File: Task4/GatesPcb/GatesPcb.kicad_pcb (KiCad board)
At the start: 2 copper layers, 73.4 x 42.7 mm, 56 parts, among them J1 Photodiode1_(+), J10 sw2, J11 sw1_PWR, J12 sw1, J13 rst_btn_gnd, J14 OTA_(+), J15 OTA_(-), J16 Laser_Mode_(-), J17 Laser_Mode_(+), J18 Btn_Mode_(-), J19 Btn_Mode_(+), J2 Photodiode1_(-), J20 Speaker_Mode_(-), J21 Speaker_Mode_(+), J22 sw2_PWR, J23 on_off_ldo, J24 rst_btn_en, J25 usr_btn_sig, J26 usr_btn_vdd, J27 Audio_P, J28 Audio_N, J3 Photodiode2_(-), J4 Photodiode2_(+), J5 on_off_bat, J6 Photodiode1Indicator_(+), J7 Photodiode1Indicator_(-), J8 Photodiode2Indicator_(+), J9 Photodiode2Indicator_(-), U1 ESP32-S2-SOLO, U2 LM317_SOT-223, U3 UART, U4 MAX98357A, U5 BOOT

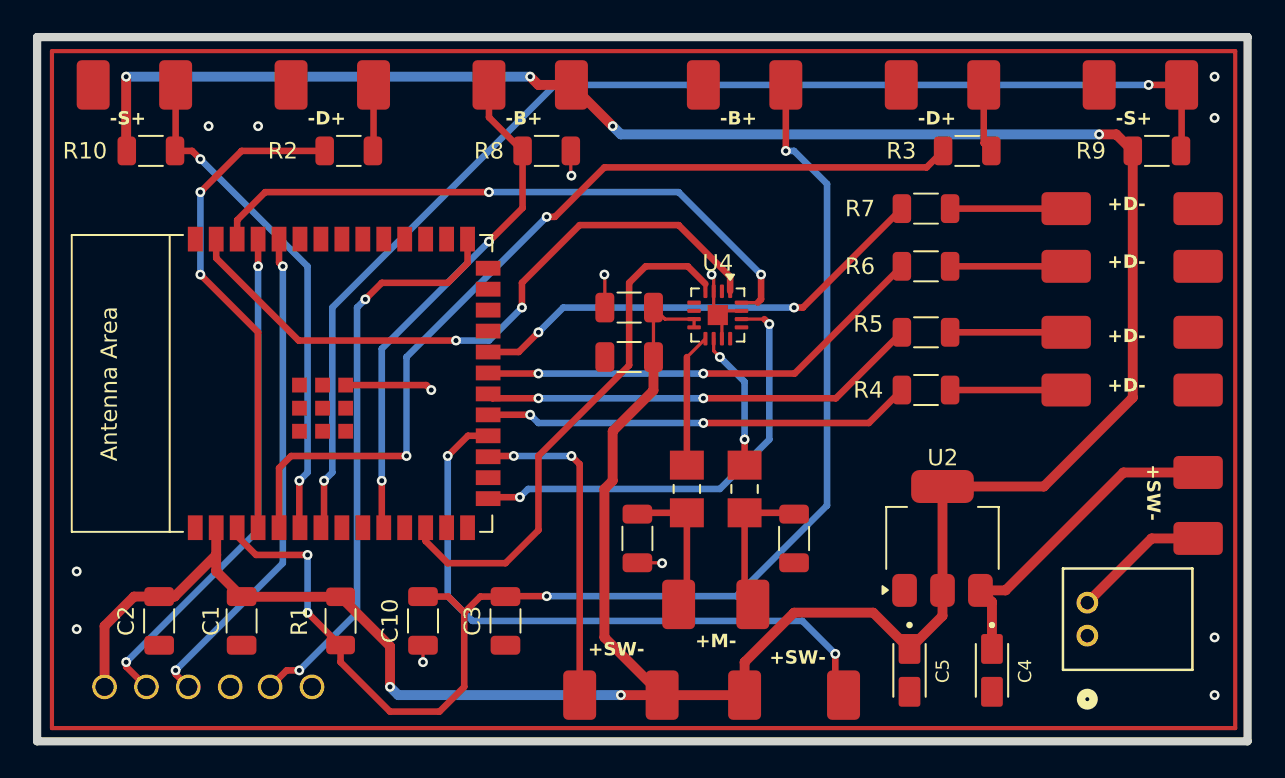
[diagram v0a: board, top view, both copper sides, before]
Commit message: pcb routing correction
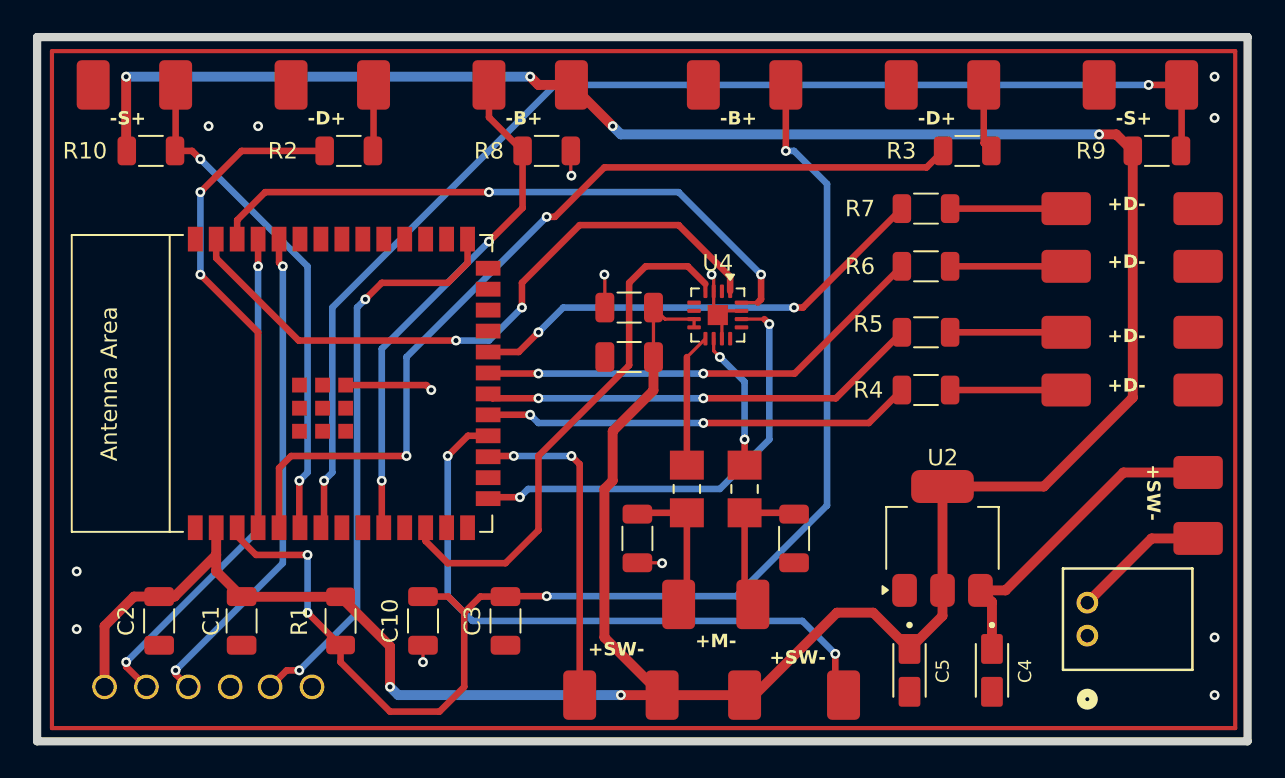
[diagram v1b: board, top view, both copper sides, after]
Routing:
- net VDD: track 201.9 -> 200.7 mm
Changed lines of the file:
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@@
-	)
-	(segment
-		(start 131.5 105)
-		(end 128.5 108)
-		(width 0.6)
-		(layer "F.Cu")
-		(net 1)
 	)
 	(segment
@@
 	)
 	(segment
+		(start 136.3 105)
+		(end 134.1 105)
+		(width 0.6)
+		(layer "F.Cu")
+		(net 1)
+	)
+	(segment
 		(start 140.5 97.35)
 		(end 140.5 103.65)
@@
 	)
 	(segment
+		(start 134.1 105)
+		(end 129.1 110)
+		(width 0.6)
+		(layer "F.Cu")
+		(net 1)
+	)
+	(segment
 		(start 125.4375 87.2)
 		(end 125.4375 87.7)
@@
 	)
 	(segment
+		(start 129.1 110)
+		(end 128.5 110)
+		(width 0.6)
+		(layer "F.Cu")
+		(net 1)
+	)
+	(segment
 		(start 123.5 110)
 		(end 121 110)
@@
 	)
 	(segment
-		(start 128.5 108)
-		(end 128.5 110)
-		(width 0.6)
-		(layer "F.Cu")
-		(net 1)
-	)
-	(segment
 		(start 152.0375 91.9625)
 		(end 152.0375 77)
@@
 	)
 	(segment
+		(start 96.46 102.485)
+		(end 96.46 101.5)
+		(width 0.6)
+		(layer "F.Cu")
+		(net 1)
+	)
+	(segment
 		(start 138.5 107.2)
 		(end 136.3 105)
-		(width 0.6)
-		(layer "F.Cu")
-		(net 1)
-	)
-	(segment
-		(start 96.46 102.485)
-		(end 96.46 101.5)
-		(width 0.6)
-		(layer "F.Cu")
-		(net 1)
-	)
-	(segment
-		(start 136.3 105)
-		(end 131.5 105)
 		(width 0.6)
 		(layer "F.Cu")
@@
 		(polygon
 			(pts
-				(xy 86.5 70.95) (xy 86.5 111.95) (xy 158.25 111.95) (xy 158.25 70.95)
+				(xy 158.25 112) (xy 158.25 70.95) (xy 86.5 70.95) (xy 86.5 112)
 			)
 		)
